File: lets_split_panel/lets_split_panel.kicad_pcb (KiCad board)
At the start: 2 copper layers, 230.5 x 82 mm, 140 parts, among them J1 Speaker, J3 ISP, J5 Speaker, J6 ISP, J7 WS2812>, J8 WS2812>, P2 USB_OTG, P3 >WS2812, P4 Conn_01x04, P5 USB_OTG, P6 >WS2812, P8 Conn_01x04, SW1 Socket, SW10 Socket, SW11 Socket, SW12 Socket, SW13 Socket, SW14 Socket, SW15 Socket, SW16 Socket, SW17 Socket, SW18 Socket, SW19 Socket, SW2 Socket, SW20 Socket, SW21 Socket, SW22 Socket, SW23 Socket, SW24 Socket, SW25 Socket, SW26 Socket, SW27 Socket, SW28 Socket, SW29 Socket, SW3 Socket, SW30 Socket, SW31 Socket, SW32 Socket, SW33 Socket, SW34 Socket, SW35 Socket, SW36 Socket, SW37 Socket, SW38 Socket, SW39 Socket, SW4 Socket, SW40 Socket, SW41 Socket, SW42 Socket, SW43 Socket, SW44 Socket, SW45 Socket, SW46 Socket, SW47 Socket, SW48 Socket, SW5 Socket, SW6 Socket, SW7 Socket, SW8 Socket, SW9 Socket, U1 ATMega32U4, U2 ATMega32U4, Y1 Crystal, Y2 Crystal

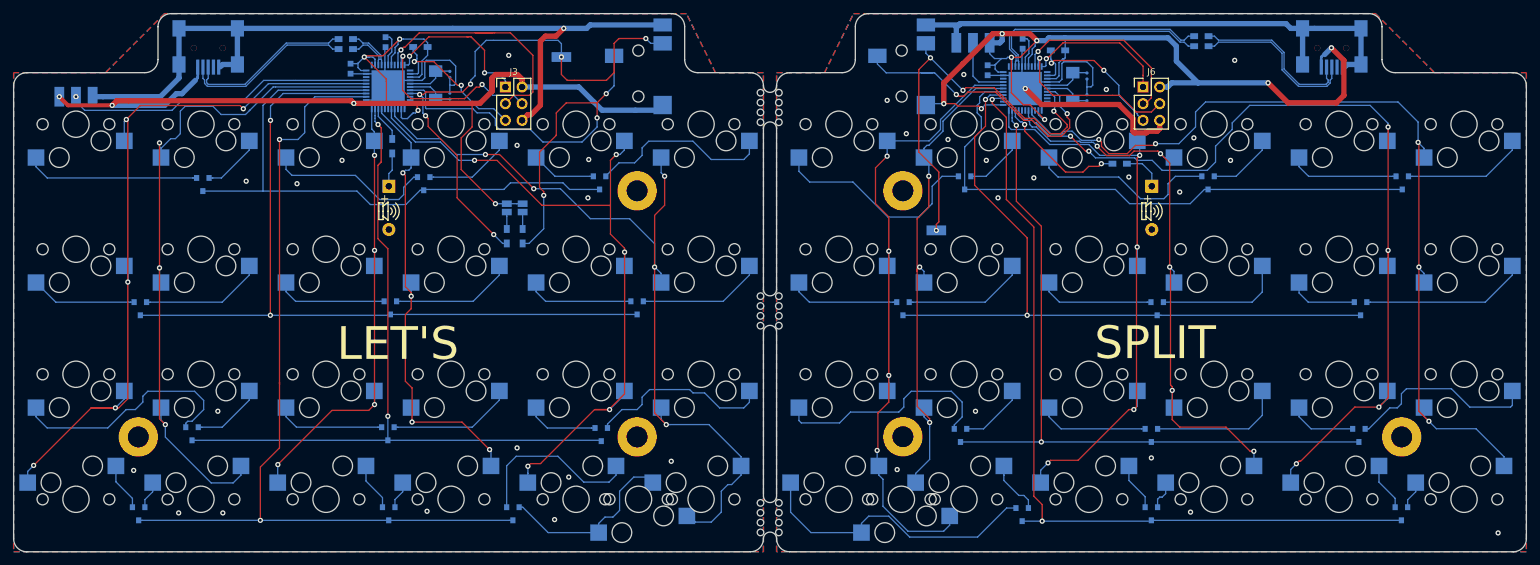
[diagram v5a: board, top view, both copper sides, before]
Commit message: Re-rendered images
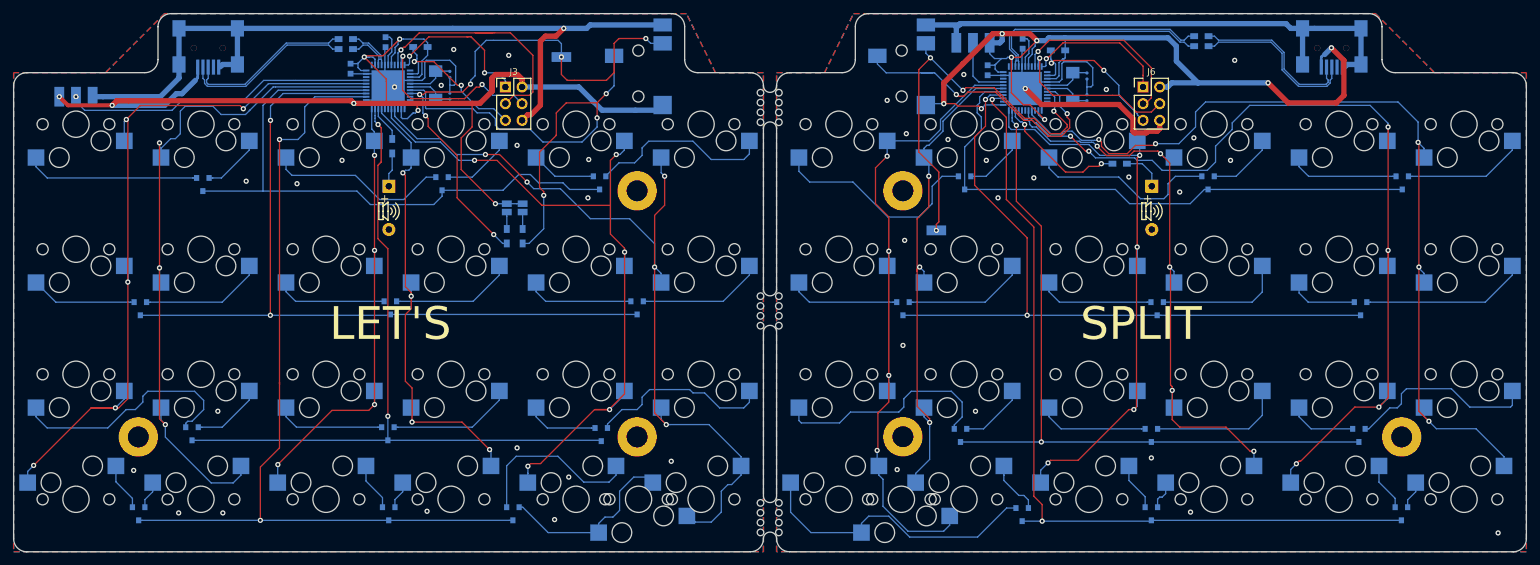
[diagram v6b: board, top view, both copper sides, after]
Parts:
- moved D2 2.79 mm to (89.3, 81.9)
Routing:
- net Net-(D2-Pad2): track 13.7 -> 10.9 mm
- net Net-(D2-Pad1): track 25.8 -> 27.9 mm
- net /Left half/row0: track 92.8 -> 94.4 mm
- net GND: vias 36 -> 41
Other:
- board text added: "I2C Pullup"
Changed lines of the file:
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@@
   (general
     (thickness 1.6)
-    (drawings 106)
-    (tracks 1491)
+    (drawings 107)
+    (tracks 1495)
     (zones 0)
     (modules 140)
@@
   )
   (setup
-    (last_trace_width 0.8128)
+    (last_trace_width 0.1524)
     (user_trace_width 0.2032)
     (user_trace_width 0.2032)
@@
   )
   (module TO_SOT_Packages_SMD:SOT-23 (layer B.Cu)
-    (at 86.487 81.915 270)
+    (at 89.281 81.915 270)
     (descr "SOT-23, Standard")
     (tags SOT-23)
@@
     )
   )
+  (gr_text "I2C\nPullup" (at 100.203 81.788) (layer B.SilkS)
+    (effects (font (size 1.5 1.5) (thickness 0.3)) (justify mirror))
+  )
   (gr_text "Original \nby \nWootpatoot" (at 217 62.75) (layer B.SilkS)
     (effects (font (size 1.5 1.5) (thickness 0.3)) (justify left mirror))
@@
     (effects (font (size 5 5) (thickness 0.3)) (justify mirror))
   )
-  (gr_text LET'S (at 82.55 106.299) (layer F.SilkS)
+  (gr_text LET'S (at 81.407 103.251) (layer F.SilkS)
     (effects (font (size 5 5) (thickness 0.3)))
   )
@@
     (effects (font (size 5 5) (thickness 0.3)) (justify mirror))
   )
-  (gr_text " SPLIT" (at 196.85 106.172) (layer F.SilkS)
+  (gr_text " SPLIT" (at 194.691 103.251) (layer F.SilkS)
     (effects (font (size 5 5) (thickness 0.3)))
   )
@@
   (gr_arc (start 139.25 73.5) (end 140.25 73.5) (angle -180) (layer Edge.Cuts) (width 0.15))
   (gr_arc (start 139.25 67) (end 138.25 67) (angle -180) (layer Edge.Cuts) (width 0.15))
+  (segment (start 93.8874 80.915) (end 90.231 80.915) (width 0.1524) (layer B.Cu) (net 2))
+  (via (at 82.042 67.183) (size 0.8) (drill 0.4) (layers F.Cu B.Cu) (net 25))
   (segment (start 101.026 131.207) (end 101.5784 131.207) (width 0.1524) (layer B.Cu) (net 12))
   (segment (start 101.5784 131.207) (end 105.4514 135.08) (width 0.1524) (layer B.Cu) (net 12))
@@
   (segment (start 174.89 124.92) (end 174.89 126.3224) (width 0.1524) (layer B.Cu) (net 22))
   (segment (start 174.89 126.3224) (end 174.879 126.3334) (width 0.1524) (layer B.Cu) (net 22))
+  (via (at 89.154 66.929) (size 0.8) (drill 0.4) (layers F.Cu B.Cu) (net 25))
+  (via (at 91.059 61.468) (size 0.8) (drill 0.4) (layers F.Cu B.Cu) (net 25))
+  (via (at 159.766 90.551) (size 0.8) (drill 0.4) (layers F.Cu B.Cu) (net 25))
+  (via (at 159.512 106.553) (size 0.8) (drill 0.4) (layers F.Cu B.Cu) (net 25))
   (segment (start 220.4 58.25) (end 220.4 63.75) (width 0.8128) (layer B.Cu) (net 25))
   (via (at 108.585 126.619) (size 0.8) (drill 0.4) (layers F.Cu B.Cu) (net 25))
@@
   (segment (start 100.6571 84.963) (end 99.1465 84.963) (width 0.1524) (layer B.Cu) (net 31))
   (segment (start 101.5595 86.233) (end 101.5595 88.816) (width 0.1524) (layer B.Cu) (net 43))
-  (segment (start 86.487 82.915) (end 86.614 82.788) (width 0.1524) (layer B.Cu) (net 47))
-  (segment (start 86.614 82.788) (end 98.695 82.788) (width 0.1524) (layer B.Cu) (net 47))
-  (segment (start 98.695 82.788) (end 99.695 81.788) (width 0.1524) (layer B.Cu) (net 47))
-  (segment (start 99.695 81.788) (end 107.712 81.788) (width 0.1524) (layer B.Cu) (net 47))
   (segment (start 107.712 81.788) (end 108.712 82.788) (width 0.1524) (layer B.Cu) (net 47))
+  (segment (start 104.013 81.788) (end 107.712 81.788) (width 0.1524) (layer B.Cu) (net 47))
+  (segment (start 102.743 80.518) (end 104.013 81.788) (width 0.1524) (layer B.Cu) (net 47))
+  (segment (start 100.965 80.518) (end 102.743 80.518) (width 0.1524) (layer B.Cu) (net 47))
+  (segment (start 89.281 82.915) (end 98.568 82.915) (width 0.1524) (layer B.Cu) (net 47))
+  (segment (start 98.568 82.915) (end 100.965 80.518) (width 0.1524) (layer B.Cu) (net 47))
   (segment (start 108.712 82.788) (end 113.284 82.788) (width 0.1524) (layer B.Cu) (net 47))
+  (segment (start 76.311 83.042) (end 78.359 85.09) (width 0.1524) (layer B.Cu) (net 47))
+  (segment (start 61.976 83.042) (end 76.311 83.042) (width 0.1524) (layer B.Cu) (net 47))
+  (segment (start 78.359 85.09) (end 88.011 85.09) (width 0.1524) (layer B.Cu) (net 47))
+  (segment (start 88.011 85.09) (end 89.281 83.82) (width 0.1524) (layer B.Cu) (net 47))
+  (segment (start 89.281 83.82) (end 89.281 82.915) (width 0.1524) (layer B.Cu) (net 47))
   (segment (start 63.119 101.965) (end 81.28 101.965) (width 0.1524) (layer B.Cu) (net 48))
   (segment (start 43.307 101.965) (end 63.119 101.965) (width 0.1524) (layer B.Cu) (net 48))
@@
   (segment (start 98.01 75.39) (end 98.01 76.7924) (width 0.1524) (layer B.Cu) (net 2))
   (segment (start 98.01 76.7924) (end 93.8874 80.915) (width 0.1524) (layer B.Cu) (net 2))
-  (segment (start 93.8874 80.915) (end 87.9894 80.915) (width 0.1524) (layer B.Cu) (net 2))
-  (segment (start 87.9894 80.915) (end 87.437 80.915) (width 0.1524) (layer B.Cu) (net 2))
   (segment (start 135.255 78.232) (end 136.11 77.377) (width 0.1524) (layer B.Cu) (net 3))
   (segment (start 136.11 77.377) (end 136.11 75.39) (width 0.1524) (layer B.Cu) (net 3))
@@
   (segment (start 177.743 59.8264) (end 178.3907 59.8264) (width 0.2032) (layer B.Cu) (net 46))
   (segment (start 61.976 83.042) (end 52.832 83.042) (width 0.1524) (layer B.Cu) (net 47))
-  (segment (start 76.311 83.042) (end 61.976 83.042) (width 0.1524) (layer B.Cu) (net 47))
   (segment (start 61.999 69.977) (end 61.999 83.019) (width 0.1524) (layer B.Cu) (net 47))
   (segment (start 61.999 83.019) (end 61.976 83.042) (width 0.1524) (layer B.Cu) (net 47))
-  (segment (start 78.359 85.09) (end 76.311 83.042) (width 0.1524) (layer B.Cu) (net 47))
-  (segment (start 83.7596 85.09) (end 78.359 85.09) (width 0.1524) (layer B.Cu) (net 47))
-  (segment (start 86.487 82.915) (end 85.9346 82.915) (width 0.1524) (layer B.Cu) (net 47))
-  (segment (start 85.9346 82.915) (end 83.7596 85.09) (width 0.1524) (layer B.Cu) (net 47))
   (segment (start 64.30516 67.67084) (end 61.999 69.977) (width 0.1524) (layer B.Cu) (net 47))
   (segment (start 77.719798 67.67084) (end 64.30516 67.67084) (width 0.1524) (layer B.Cu) (net 47))
@@
   (via (at 102.362 124.968) (size 0.8) (drill 0.4) (layers F.Cu B.Cu) (net 81))
   (segment (start 81.565358 70.52072) (end 81.565358 71.890358) (width 0.1524) (layer B.Cu) (net 81))
+  (segment (start 95.885 77.47) (end 98.044 77.47) (width 0.1524) (layer F.Cu) (net 82))
+  (segment (start 98.044 77.47) (end 102.235 81.661) (width 0.1524) (layer F.Cu) (net 82))
+  (segment (start 103.251 82.677) (end 102.235 81.661) (width 0.1524) (layer B.Cu) (net 82))
+  (via (at 102.235 81.661) (size 0.8) (drill 0.4) (layers F.Cu B.Cu) (net 82))
   (segment (start 127.889 133.477) (end 130.302 133.477) (width 0.1524) (layer B.Cu) (net 82))
   (segment (start 130.302 133.477) (end 131.826 131.953) (width 0.1524) (layer B.Cu) (net 82))
@@
   (segment (start 117.856 87.249) (end 121.666 91.059) (width 0.1524) (layer B.Cu) (net 82))
   (segment (start 121.666 91.059) (end 121.666 94.615) (width 0.1524) (layer B.Cu) (net 82))
-  (segment (start 98.044 77.47) (end 103.251 82.677) (width 0.1524) (layer F.Cu) (net 82))
-  (segment (start 96.450685 77.47) (end 98.044 77.47) (width 0.1524) (layer F.Cu) (net 82))
-  (via (at 103.251 82.677) (size 0.8) (drill 0.4) (layers F.Cu B.Cu) (net 82))
-  (segment (start 95.885 77.47) (end 96.450685 77.47) (width 0.1524) (layer F.Cu) (net 82))
   (segment (start 91.44 77.47) (end 95.885 77.47) (width 0.1524) (layer B.Cu) (net 82))
   (segment (start 89.027 75.057) (end 91.44 77.47) (width 0.1524) (layer B.Cu) (net 82))
@@
   (segment (start 29.1196 81.042) (end 51.3296 81.042) (width 0.1524) (layer B.Cu) (net 103))
   (segment (start 51.3296 81.042) (end 51.882 81.042) (width 0.1524) (layer B.Cu) (net 103))
+  (segment (start 82.677 84.328) (end 83.439 84.328) (width 0.1524) (layer B.Cu) (net 104))
+  (segment (start 83.439 84.328) (end 86.852 80.915) (width 0.1524) (layer B.Cu) (net 104))
+  (segment (start 88.331 80.915) (end 86.852 80.915) (width 0.1524) (layer B.Cu) (net 104))
   (segment (start 66.421 80.645) (end 65.51 79.734) (width 0.1524) (layer B.Cu) (net 104))
   (segment (start 65.51 79.734) (end 65.51 77.93) (width 0.1524) (layer B.Cu) (net 104))
@@
   (segment (start 79.756 84.328) (end 76.073 80.645) (width 0.1524) (layer B.Cu) (net 104))
   (segment (start 82.677 84.328) (end 79.756 84.328) (width 0.1524) (layer B.Cu) (net 104))
-  (segment (start 83.439 83.566) (end 82.677 84.328) (width 0.1524) (layer B.Cu) (net 104))
-  (segment (start 83.439 82.4606) (end 83.439 83.566) (width 0.1524) (layer B.Cu) (net 104))
-  (segment (start 85.537 80.915) (end 84.9846 80.915) (width 0.1524) (layer B.Cu) (net 104))
-  (segment (start 84.9846 80.915) (end 83.439 82.4606) (width 0.1524) (layer B.Cu) (net 104))
   (segment (start 103.61 77.93) (end 103.635 77.93) (width 0.1524) (layer B.Cu) (net 105))
   (segment (start 103.635 77.93) (end 106.493 80.788) (width 0.1524) (layer B.Cu) (net 105))

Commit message: Added fancy :)
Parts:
- added G***: LOGO, graphics:NovelKeys, B.Cu at (219.2, 86.8)
- added G***: LOGO, graphics:NovelKeys, B.Cu at (40.4, 86.6)
- C1, C4, C5, C8: footprint SeeedOPL-Capacitor-2016:C0603 -> Capacitors_SMD:C_0603
- C2, C3, C6, C7: footprint SeeedOPL-Capacitor-2016:C0402 -> Capacitors_SMD:C_0603
- R1, R10, R2, R3, R4, R5, R6, R7, R8, R9: footprint Resistors_SMD:R_0603_HandSoldering -> Resistors_SMD:R_0603
- Y1, Y2: footprint SeeedOPL-Crystal Oscillator-2016:X2-SMD-5.0X3.2X1.3MM -> SeeedOPL-Crystal Oscillator-2016:X2-SMD-3.2X1.5X0.55MM
- moved R10 7.28 mm to (186.2, 82.4)
- moved C2 0.88 mm to (90.4, 67.7), turned to 90 degrees
- moved C6 0.86 mm to (187.6, 67.9), turned to 90 degrees
- moved C7 0.61 mm to (187.6, 64.9), turned to 90 degrees
- moved C3 0.50 mm to (90.4, 64.8), turned to 90 degrees
- turned C1 to 270 degrees
- turned C4 to 270 degrees
- turned C5 to 270 degrees
- turned C8 to 270 degrees
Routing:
- net GND: track 314.0 -> 308.9 mm
- net /Right half/buzz: track 21.3 -> 16.6 mm
- net Net-(J5-Pad1): track 6.36 -> 10.5 mm
- net Net-(D14-Pad1): track 29.2 -> 30.8 mm
- net /Right half/row0: track 88.0 -> 88.6 mm
- net Net-(JP2-Pad2): track 2.58 -> 3.23 mm
- net Net-(JP1-Pad2): track 2.58 -> 3.23 mm
- net Net-(C3-Pad1): track 7.50 -> 6.86 mm
- net Net-(C2-Pad1): track 7.43 -> 6.80 mm
- net VBUS: track 346.6 -> 346.0 mm
- net Net-(C7-Pad1): track 7.50 -> 6.89 mm
- net Net-(C6-Pad1): track 7.43 -> 6.89 mm
- net /Left half/~Reset: track 24.5 -> 24.0 mm
- net /Right half/Dd-: track 25.3 -> 25.8 mm
- net /Right half/Dd+: track 25.8 -> 26.3 mm
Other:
- rule via_min_drill: 0.3 -> 0.4
- rule via_min_size: 0.4 -> 0.8
- board text added: "Designed made in Denmark, EU"
- board text added: "Made in partnership with"
- board text added: "and"
- board text added: "git.io/vbUi0"

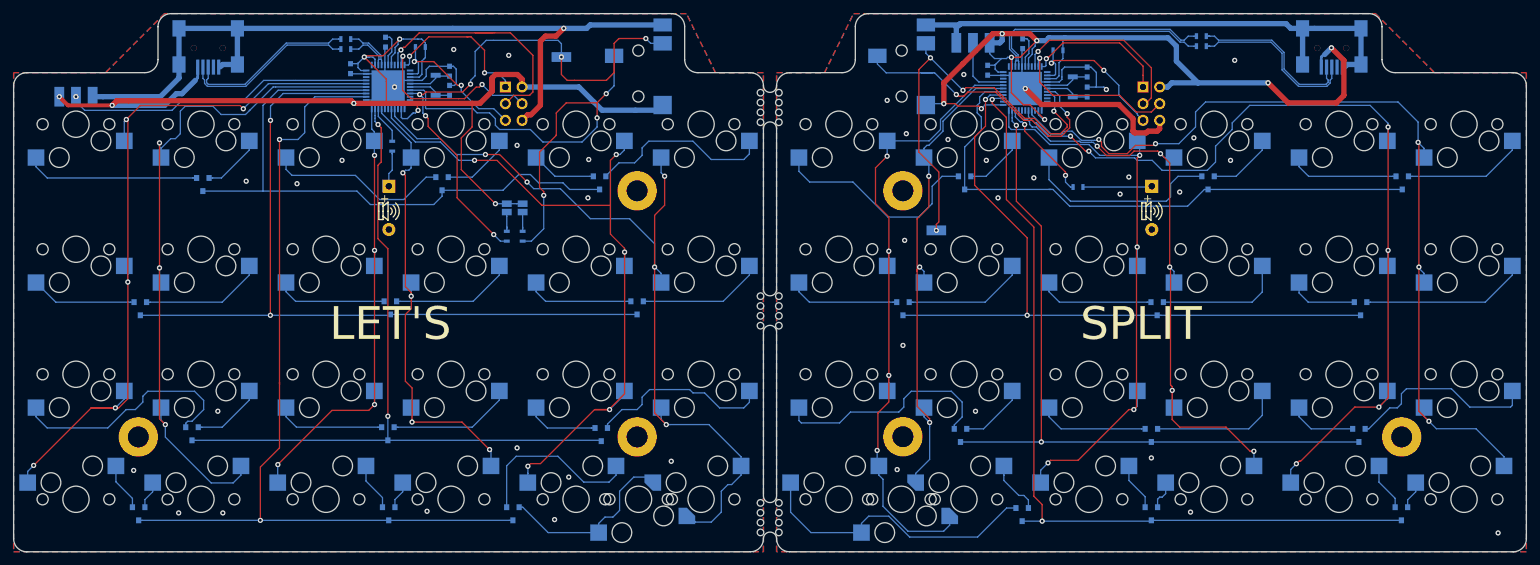
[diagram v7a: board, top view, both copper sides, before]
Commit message: Finished programming jig
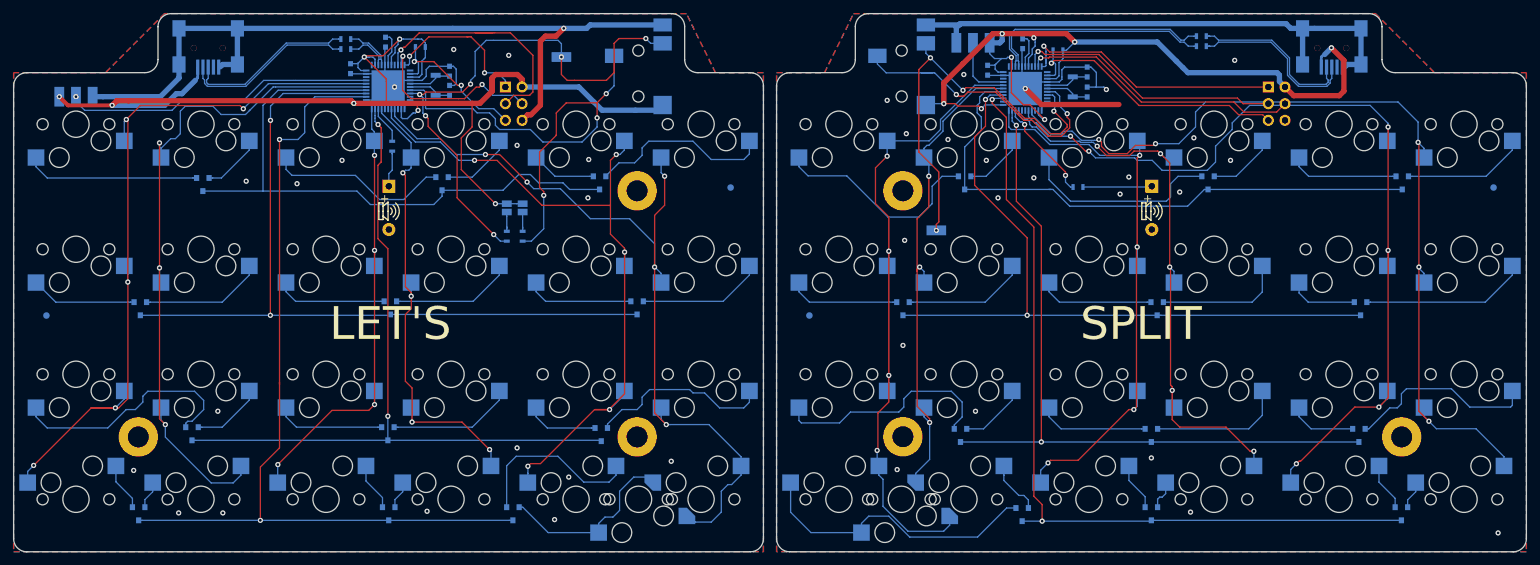
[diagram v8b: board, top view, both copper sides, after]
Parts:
- removed the REF** at (137.8, 103.5)
- removed the REF** at (140.6, 102.0)
- removed the REF** at (140.6, 132.1)
- removed the REF** at (137.8, 133.6)
- removed the REF** at (137.8, 130.6)
- removed the REF** at (137.8, 132.1)
- removed the REF** at (137.8, 135.1)
- removed the REF** at (140.6, 130.6)
- removed the REF** at (140.6, 135.1)
- removed the REF** at (140.6, 133.6)
- removed the REF** at (140.6, 71.0)
- removed the REF** at (140.6, 68.0)
- removed the REF** at (137.8, 68.0)
- removed the REF** at (137.8, 72.5)
- removed the REF** at (140.6, 72.5)
- removed the REF** at (137.8, 71.0)
- removed the REF** at (137.8, 69.5)
- removed the REF** at (140.6, 69.5)
- removed the REF** at (140.6, 100.5)
- removed the REF** at (137.8, 100.5)
- removed the REF** at (137.8, 102.0)
- removed the REF** at (140.6, 103.5)
- removed the REF** at (140.6, 99.0)
- removed the REF** at (137.8, 99.0)
- added REF**: Fiducial_1mm_Dia_2mm_Outer, Fiducials:Fiducial_1mm_Dia_2mm_Outer, B.Cu at (249.5, 82.5)
- added REF**: Fiducial_1mm_Dia_2mm_Outer, Fiducials:Fiducial_1mm_Dia_2mm_Outer, B.Cu at (133.2, 82.5)
- added REF**: Fiducial_1mm_Dia_2mm_Outer, Fiducials:Fiducial_1mm_Dia_2mm_Outer, B.Cu at (145.2, 102.0)
- added REF**: Fiducial_1mm_Dia_2mm_Outer, Fiducials:Fiducial_1mm_Dia_2mm_Outer, B.Cu at (29.0, 102.0)
- moved J6 19.1 mm to (215.2, 67.2)
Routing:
- net /Right half/MISO: track 22.2 -> 41.2 mm
- net /Right half/~RESET: track 24.7 -> 42.8 mm, vias 2 -> 1
- net /Right half/MOSI: track 25.7 -> 42.7 mm
- net /Right half/SCK: track 28.4 -> 40.9 mm
- net VBUS: track 346.0 -> 333.9 mm
- net GND: track 308.9 -> 298.2 mm
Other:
- outline, holes or cut-outs redrawn
